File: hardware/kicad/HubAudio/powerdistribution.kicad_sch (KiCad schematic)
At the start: 80 parts, among them U14 TPS22919DCK, U21 TPS22919DCK, U22 TPS22919DCK, U23 TPS22919DCK, U26 TPS22919DCK, U27 TPS22919DCK, U31 TPS22919DCK, U32 TPS22919DCK, U33 TPS22919DCK, U9 TPS22919DCK

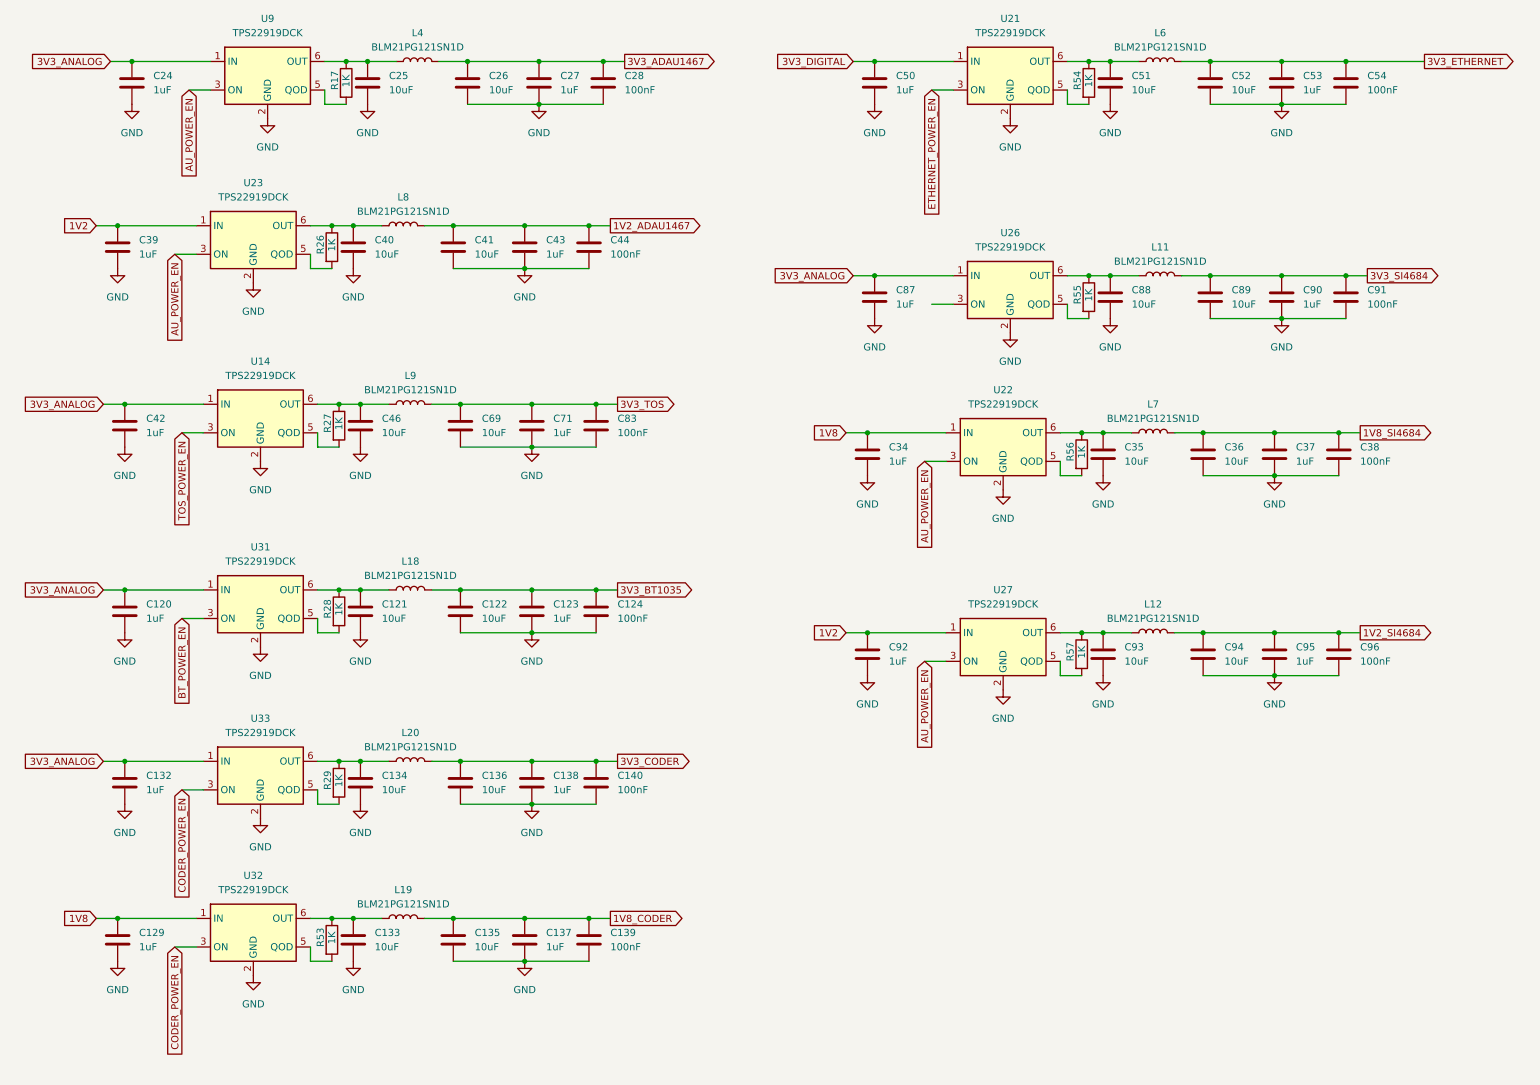
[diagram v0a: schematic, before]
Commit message: Finalize I2C and SPI control architecture
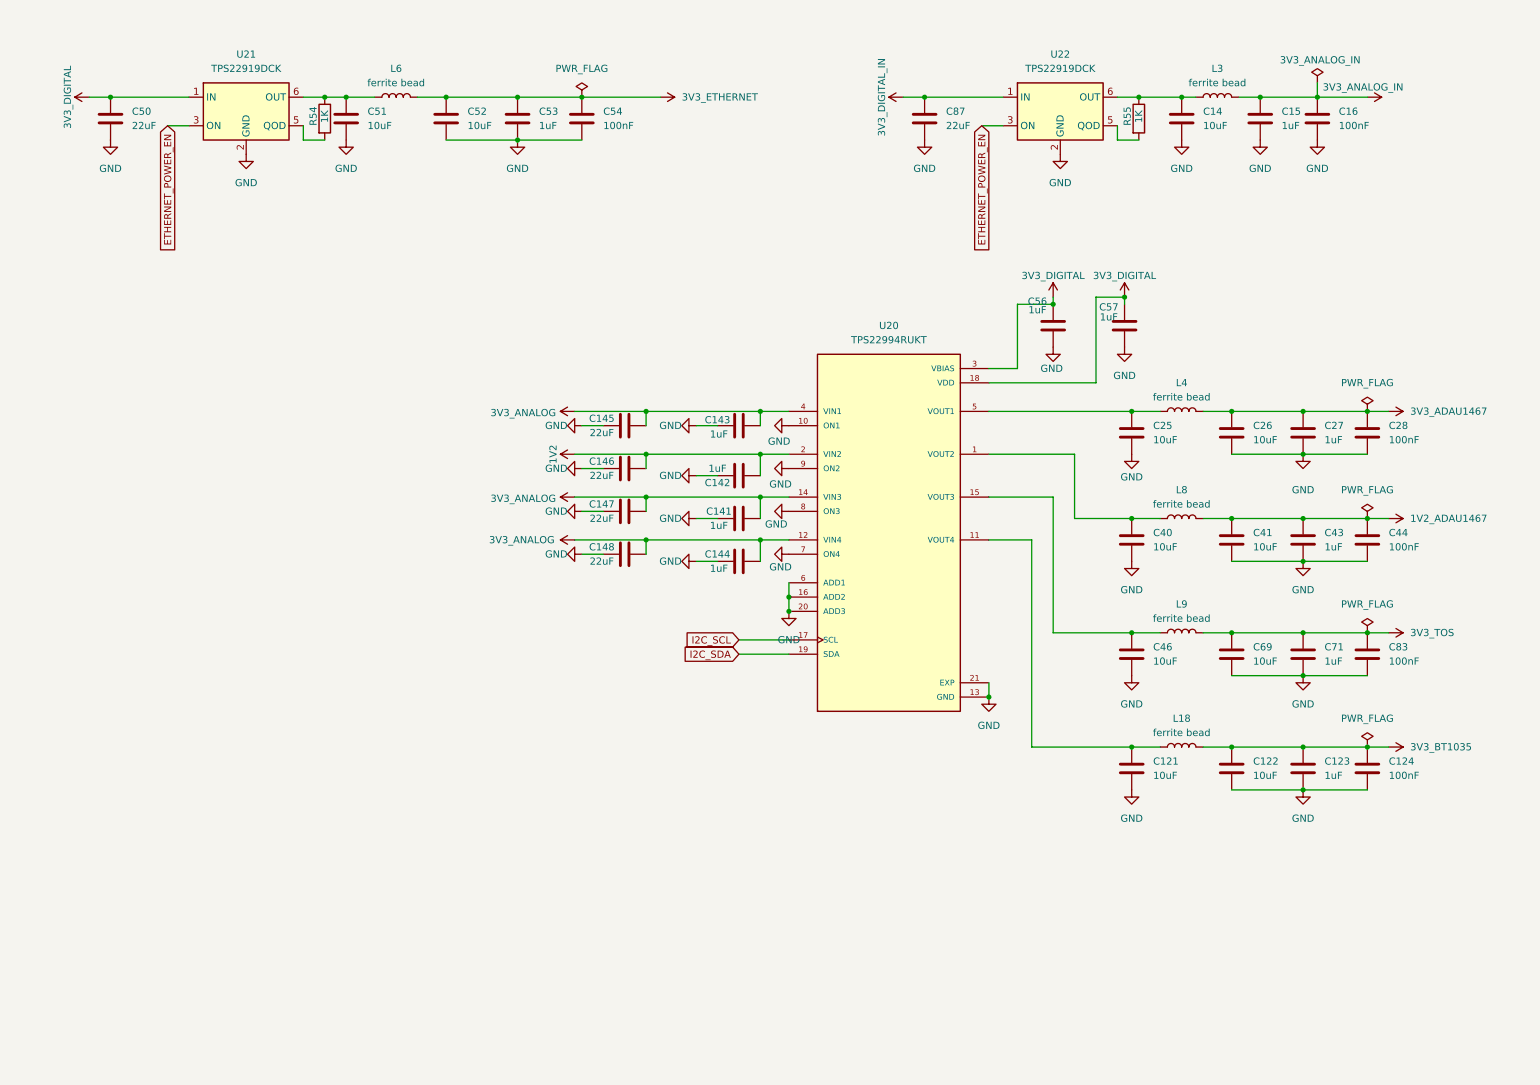
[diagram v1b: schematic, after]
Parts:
- removed C120, C129, C132, C137, C138, C24, C34, C37, C39, C42, C90, C92, C95: 1uF, Capacitor_SMD:C_0805_2012Metric, symbol Device:C
- removed C133, C134, C135, C136, C35, C36, C88, C89, C93, C94: 10uF, Capacitor_SMD:C_1206_3216Metric, symbol Device:C
- removed C139, C140, C38, C91, C96: 100nF, Capacitor_SMD:C_0805_2012Metric, symbol Device:C
- removed L11, L12, L19, L20, L7: BLM21PG121SN1D, Inductor_SMD:L_0805_2012Metric, symbol Device:L
- removed R17, R26, R27, R28, R29, R53, R56, R57: 1K, Resistor_SMD:R_0805_2012Metric, symbol Device:R
- removed U14, U23, U26, U27, U31, U32, U33, U9: TPS22919DCK, Package_TO_SOT_SMD:SOT-363_SC-70-6, symbol Power_Management:TPS22919DCK
- added C14: 10uF, Capacitor_SMD:C_1206_3216Metric, symbol Device:C
- added C141, C142, C143, C144, C56, C57: 1uF, Capacitor_SMD:C_0805_2012Metric, symbol Device:C
- added C145, C146, C147, C148: 22uF, Capacitor_SMD:C_0805_2012Metric, symbol Device:C
- added C15: 1uF, Capacitor_SMD:C_1206_3216Metric, symbol Device:C
- added C16: 100nF, Capacitor_SMD:C_0805_2012Metric, symbol Device:C
- added L3: ferrite bead, Inductor_SMD:L_0805_2012Metric, symbol Device:L
- added U20: TPS22994RUKT, MIKILAB_TPS22994RUKT:IC_TPS22994RUKT, symbol MIKILAB_TPS22994RUKT:TPS22994RUKT
- C121, C122, C25, C26, C40, C41, C46, C51, C52, C69: PNM (none) -> GRM31CR71E106KA12L
- C123, C27, C43, C53, C71: PNM (none) -> GCM21BR71E105KA56L
- C124, C28, C44, C54, C83: PNM (none) -> GRM21BR71H104KA01L
- C50, C87: value 1uF -> 22uF; PNM (none) -> GRM21BZ71A226ME15L
- L18, L4, L6, L8, L9: value BLM21PG121SN1D -> ferrite bead; PNM (none) -> BLM21PG121SN1D
- R54, R55: PNM (none) -> MCR10EZHF1001
- U21, U22: PNM (none) -> TPS22919DCK
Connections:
- net AU_POWER_EN is gone; now on net ETHERNET_POWER_EN: U22.3 (ON)
- net 1V2: now also C142.2, C146.2, U20.2 (VIN2)
- net 3V3_ANALOG: now also C141.1, C143.1, C144.1, C145.2, C147.2, C148.2, U20.12 (VIN4), U20.14 (VIN3), U20.4 (VIN1); no longer C87.1
- net 3V3_DIGITAL: now also C56.2, C57.2, U20.18 (VDD), U20.3 (VBIAS)
- net GND: now also C14.2, C141.2, C142.1, C143.2, C144.2, C145.1, C146.1, C147.1, C148.1, C15.2, C16.2, C56.1, C57.1, U20.10 (ON1), U20.13 (GND), U20.16 (ADD2), U20.20 (ADD3), U20.21 (EXP), U20.6 (ADD1), U20.7 (ON4), U20.8 (ON3), U20.9 (ON2)
- net at C40.1, L8.1: now also U20.1 (VOUT2)
- net at R55.1: now also U22.6 (OUT), C14.1, L3.1
- net at C121.1, L18.1: now also U20.11 (VOUT4)
- net at R55.2: now also U22.5 (QOD)
- net at C25.1, L4.1: now also U20.5 (VOUT1)
- net at C46.1, L9.1: now also U20.15 (VOUT3)
- net 1V8 renamed 3V3_DIGITAL_IN
- net 3V3_DIGITAL_IN: now also C87.1
- new net 3V3_ANALOG_IN: C15.1, C16.1, L3.2
- new net I2C_SCL: U20.17 (SCL)
- new net I2C_SDA: U20.19 (SDA)
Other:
- moved on the sheet: C51, C52, C53, C54, L6, R54, U21

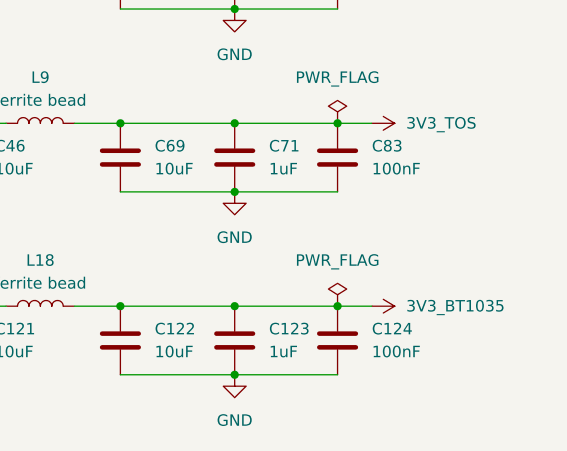
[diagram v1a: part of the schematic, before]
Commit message: Finalize HubAudio hardware architecture and PCB
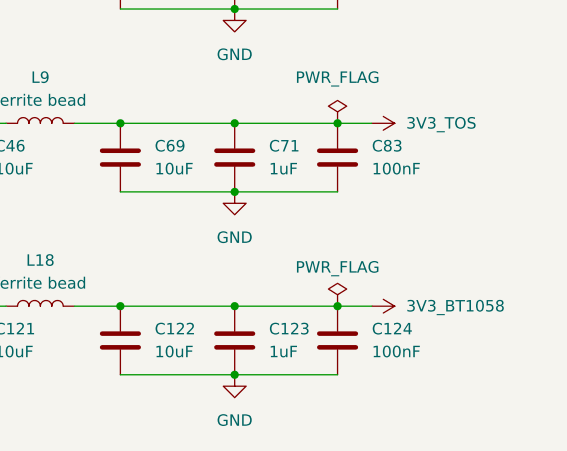
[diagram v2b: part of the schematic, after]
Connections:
- net 3V3_BT1035 renamed 3V3_BT1058
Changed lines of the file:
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@@
 		(in_pos_files yes)
 		(dnp no)
-		(fields_autoplaced yes)
 		(property "Reference" "#FLG010"
 			(at 256.54 144.145 0)
@@
 		)
 		(property "Value" "PWR_FLAG"
-			(at 256.54 140.97 0)
+			(at 256.54 141.732 0)
 			(show_name no)
 			(do_not_autoplace no)
@@
 			)
 		)
-		(property "Value" "3V3_BT1035"
+		(property "Value" "3V3_BT1058"
 			(at 264.16 146.0499 90)
 			(show_name no)
